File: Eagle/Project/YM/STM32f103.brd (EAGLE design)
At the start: 174.2 x 88.8 mm, 81 parts, among them IC1 YM3812, IC10 YM3812, IC11 YM3014B, IC12 LM358N, IC13 BA033CC0T, IC14 74ALS04N, IC15 6N136, IC2 YM3014B, IC3 LM358N, IC4 YM3812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

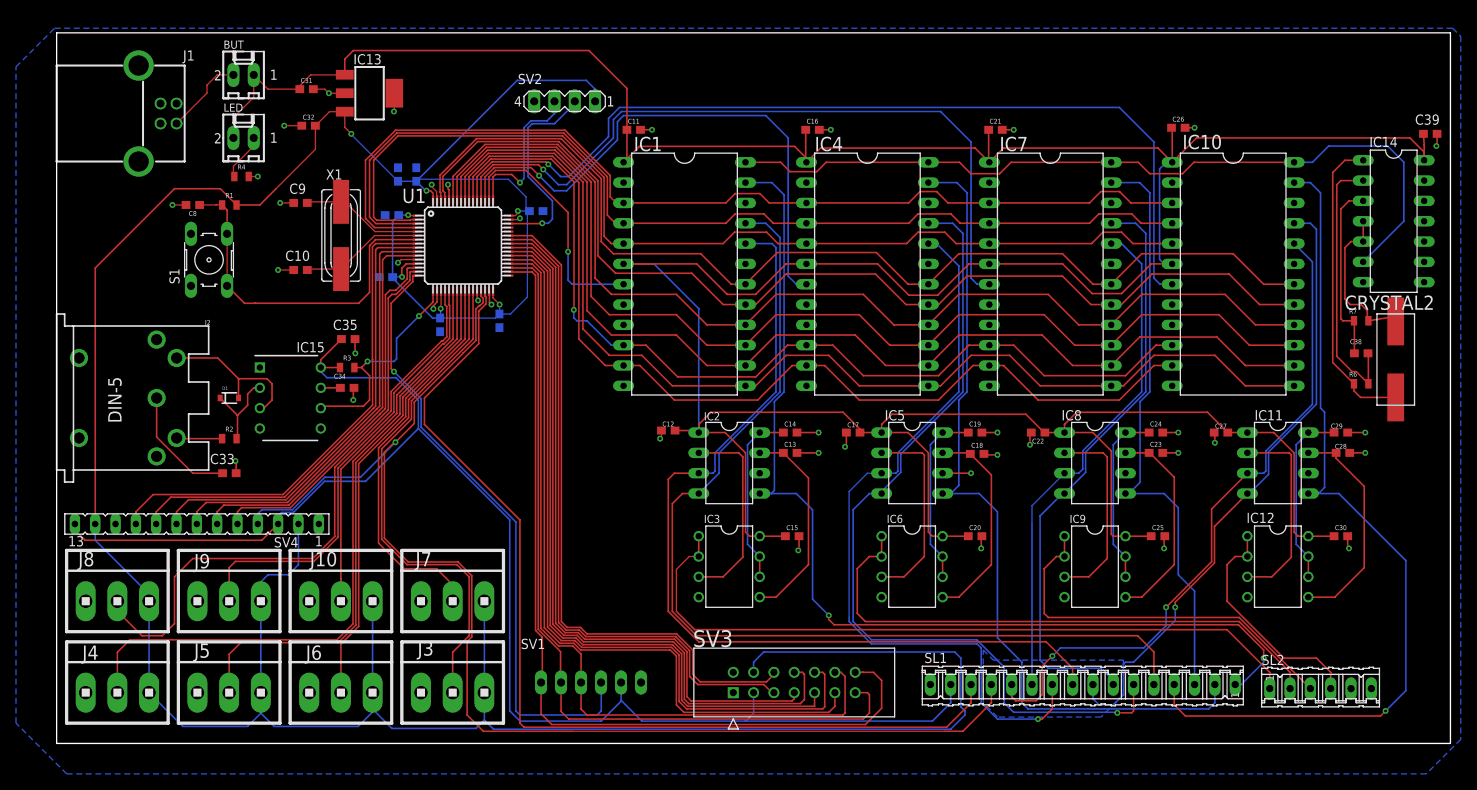
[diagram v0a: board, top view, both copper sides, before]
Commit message: Schroefgaten toegevoegd
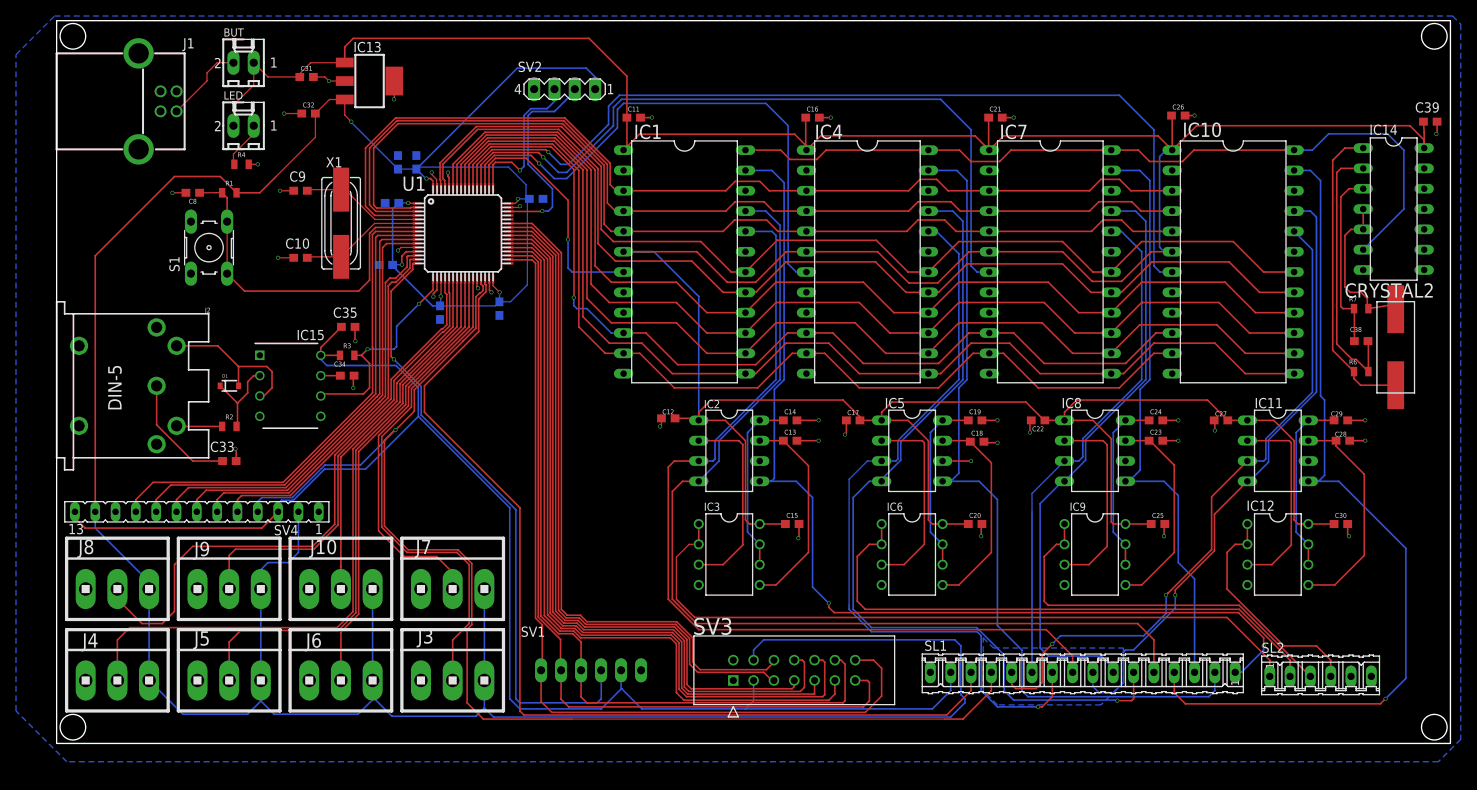
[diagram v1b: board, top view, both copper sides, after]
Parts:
- moved BUT 1.52 mm to (23.4, 85.1)
- moved C1 1.52 mm to (42.7, 72.6)
- moved C10 1.52 mm to (30.5, 60.7)
- moved C11 1.52 mm to (72.1, 78.2)
- moved C12 1.52 mm to (76.5, 40.6)
- moved C14 1.52 mm to (91.7, 40.4)
- moved C16 1.52 mm to (94.5, 78.2)
- moved C17 1.52 mm to (99.6, 40.4)
- moved C18 1.52 mm to (115.1, 37.7)
- moved C19 1.52 mm to (114.8, 40.4)
- moved C21 1.52 mm to (117.3, 78.2)
- moved C22 1.52 mm to (122.7, 40.4)
- moved C24 1.52 mm to (137.4, 40.4)
- moved C26 1.52 mm to (140.2, 78.5)
- moved C27 1.52 mm to (145.5, 40.4)
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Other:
- board size 174.2 x 88.8 mm -> 174.2 x 90.3 mm

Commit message: review door Ruben met een paar changes
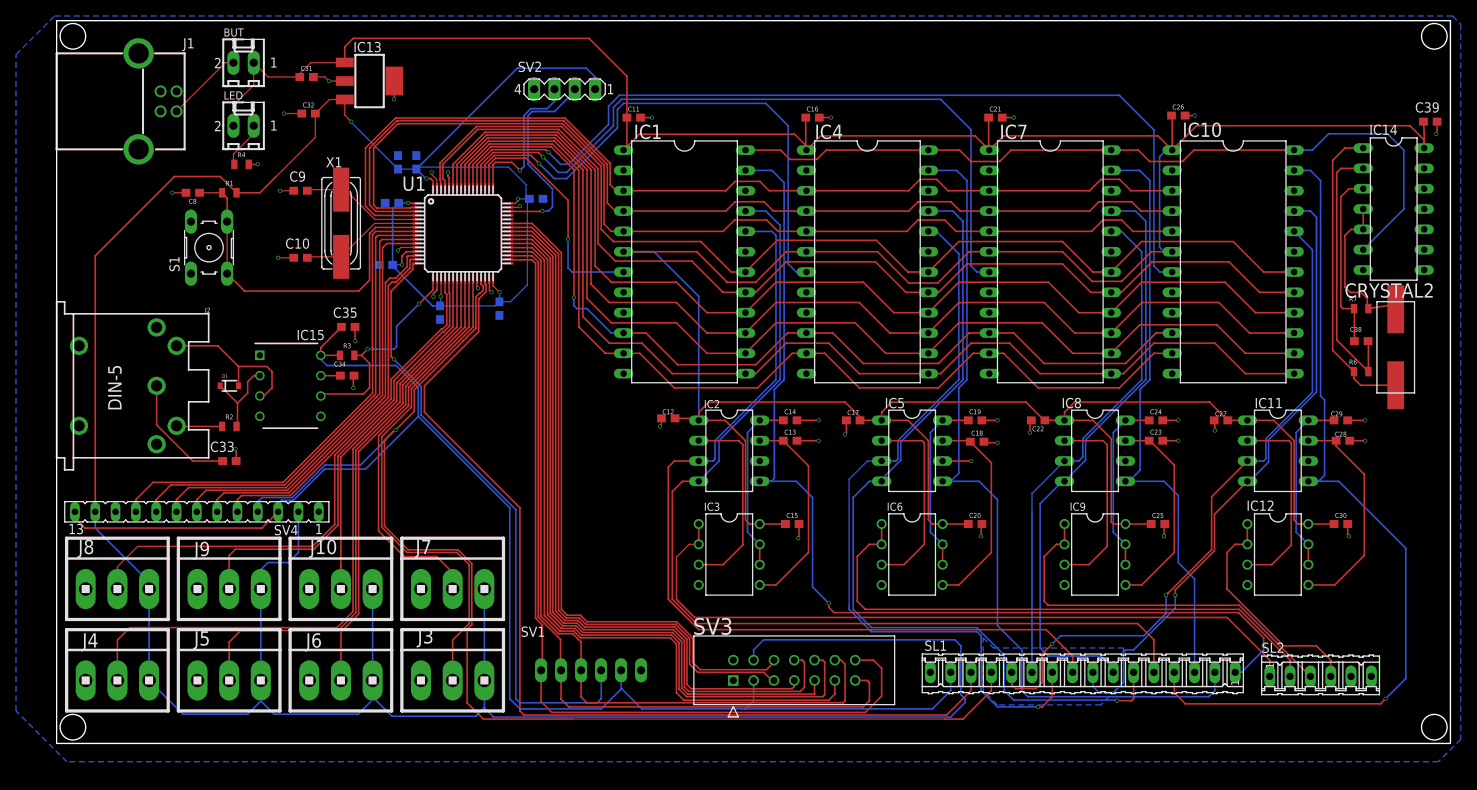
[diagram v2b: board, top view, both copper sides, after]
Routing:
- net ADC1: track 74.9 -> 68.8 mm
- net 5VBUTTON: track 10.2 -> 9.62 mm
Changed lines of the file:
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@@
 <?xml version="1.0" encoding="utf-8"?>
 <!DOCTYPE eagle SYSTEM "eagle.dtd">
-<eagle version="9.5.1">
+<eagle version="9.5.2">
 <drawing>
 <settings>
@@
 <wire x1="34.7648" y1="36.0399" x2="34.7648" y2="27.3988" width="0.2032" layer="1"/>
 <wire x1="32.004" y1="24.638" x2="34.7648" y2="27.3988" width="0.2032" layer="1"/>
-<wire x1="7.5946" y1="19.304" x2="7.5946" y2="18.0594" width="0.2032" layer="1"/>
-<wire x1="10.668" y1="14.986" x2="13.208" y2="14.986" width="0.2032" layer="1"/>
-<wire x1="13.208" y1="14.986" x2="14.732" y2="16.51" width="0.2032" layer="1"/>
-<wire x1="14.732" y1="22.352" x2="17.018" y2="24.638" width="0.2032" layer="1"/>
-<wire x1="17.018" y1="24.638" x2="32.004" y2="24.638" width="0.2032" layer="1"/>
-<wire x1="7.5946" y1="18.0594" x2="10.668" y2="14.986" width="0.2032" layer="1"/>
-<wire x1="14.732" y1="16.51" x2="14.732" y2="22.352" width="0.2032" layer="1"/>
+<wire x1="32.004" y1="24.638" x2="17.018" y2="24.638" width="0.2032" layer="1"/>
+<wire x1="17.018" y1="24.638" x2="10.1346" y2="24.638" width="0.1524" layer="1"/>
+<wire x1="10.1346" y1="24.638" x2="7.5946" y2="22.098" width="0.1524" layer="1"/>
+<wire x1="7.5946" y1="22.098" x2="7.5946" y2="19.304" width="0.1524" layer="1"/>
 </signal>
 <signal name="ADC2">
@@
 <wire x1="83.566" y1="40.386" x2="86.106" y2="37.846" width="0.2032" layer="1"/>
 <wire x1="103.124" y1="40.386" x2="100.418" y2="40.386" width="0.2032" layer="1"/>
-<wire x1="98.298" y1="42.926" x2="100.418" y2="40.806" width="0.2032" layer="1"/>
+<wire x1="98.552" y1="42.672" x2="100.418" y2="40.806" width="0.2032" layer="1"/>
 <wire x1="100.418" y1="40.806" x2="100.418" y2="40.386" width="0.2032" layer="1"/>
 <wire x1="103.124" y1="40.386" x2="106.426" y2="40.386" width="0.2032" layer="1"/>
@@
 <wire x1="136.818" y1="27.432" x2="133.604" y2="27.432" width="0.2032" layer="1"/>
 <wire x1="125.984" y1="40.386" x2="125.984" y2="41.402" width="0.2032" layer="1"/>
-<wire x1="125.984" y1="41.402" x2="127.508" y2="42.926" width="0.2032" layer="1"/>
-<wire x1="127.508" y1="42.926" x2="143.852" y2="42.926" width="0.2032" layer="1"/>
-<wire x1="143.852" y1="42.926" x2="146.392" y2="40.386" width="0.2032" layer="1"/>
+<wire x1="125.984" y1="41.402" x2="127.254" y2="42.672" width="0.2032" layer="1"/>
+<wire x1="127.254" y1="42.672" x2="144.106" y2="42.672" width="0.2032" layer="1"/>
+<wire x1="144.106" y1="42.672" x2="146.392" y2="40.386" width="0.2032" layer="1"/>
 <wire x1="146.392" y1="40.386" x2="148.844" y2="40.386" width="0.2032" layer="1"/>
 <wire x1="159.678" y1="27.432" x2="156.464" y2="27.432" width="0.2032" layer="1"/>
@@
 <contactref element="SV3" pad="3"/>
 <wire x1="80.264" y1="40.386" x2="80.264" y2="41.402" width="0.2032" layer="1"/>
-<wire x1="81.788" y1="42.926" x2="80.264" y2="41.402" width="0.2032" layer="1"/>
-<wire x1="81.788" y1="42.926" x2="98.298" y2="42.926" width="0.2032" layer="1"/>
+<wire x1="81.534" y1="42.672" x2="80.264" y2="41.402" width="0.2032" layer="1"/>
+<wire x1="81.534" y1="42.672" x2="98.552" y2="42.672" width="0.2032" layer="1"/>
 <contactref element="SV4" pad="13"/>
 <contactref element="SV4" pad="3"/>
@@
 <contactref element="IC14" pad="2"/>
 <contactref element="C38" pad="2"/>
-<wire x1="160.02" y1="49.922" x2="160.02" y2="71.374" width="0.2032" layer="1"/>
+<wire x1="160.02" y1="50.43" x2="160.02" y2="71.374" width="0.2032" layer="1"/>
 <wire x1="160.02" y1="71.374" x2="160.528" y2="71.882" width="0.2032" layer="1"/>
 <wire x1="160.528" y1="71.882" x2="163.322" y2="71.882" width="0.2032" layer="1"/>
-<wire x1="163.968" y1="46.482" x2="162.444" y2="48.006" width="0.2032" layer="1"/>
-<wire x1="161.936" y1="48.006" x2="160.02" y2="49.922" width="0.2032" layer="1"/>
-<wire x1="162.444" y1="48.006" x2="161.936" y2="48.006" width="0.2032" layer="1"/>
+<wire x1="163.968" y1="46.482" x2="160.02" y2="50.43" width="0.2032" layer="1"/>
 <wire x1="163.968" y1="46.482" x2="163.968" y2="50.242" width="0.2032" layer="1"/>
 <wire x1="163.968" y1="50.242" x2="163.918" y2="50.292" width="0.2032" layer="1"/>
@@
 <contactref element="J1" pad="1"/>
 <contactref element="BUT" pad="2"/>
-<wire x1="14.9901" y1="79.0141" x2="18.796" y2="82.82" width="0.1524" layer="1"/>
-<wire x1="18.796" y1="82.82" x2="18.796" y2="83.82" width="0.1524" layer="1"/>
-<wire x1="18.796" y1="83.82" x2="20.066" y2="85.09" width="0.1524" layer="1"/>
-<wire x1="20.066" y1="85.09" x2="22.098" y2="85.09" width="0.1524" layer="1"/>
+<wire x1="14.9901" y1="79.0141" x2="21.066" y2="85.09" width="0.1524" layer="1"/>
+<wire x1="21.066" y1="85.09" x2="22.098" y2="85.09" width="0.1524" layer="1"/>
 </signal>
 <signal name="N$13">
